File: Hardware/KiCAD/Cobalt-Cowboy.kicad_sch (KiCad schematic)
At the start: 1 part, among them P1 USB_C_Plug

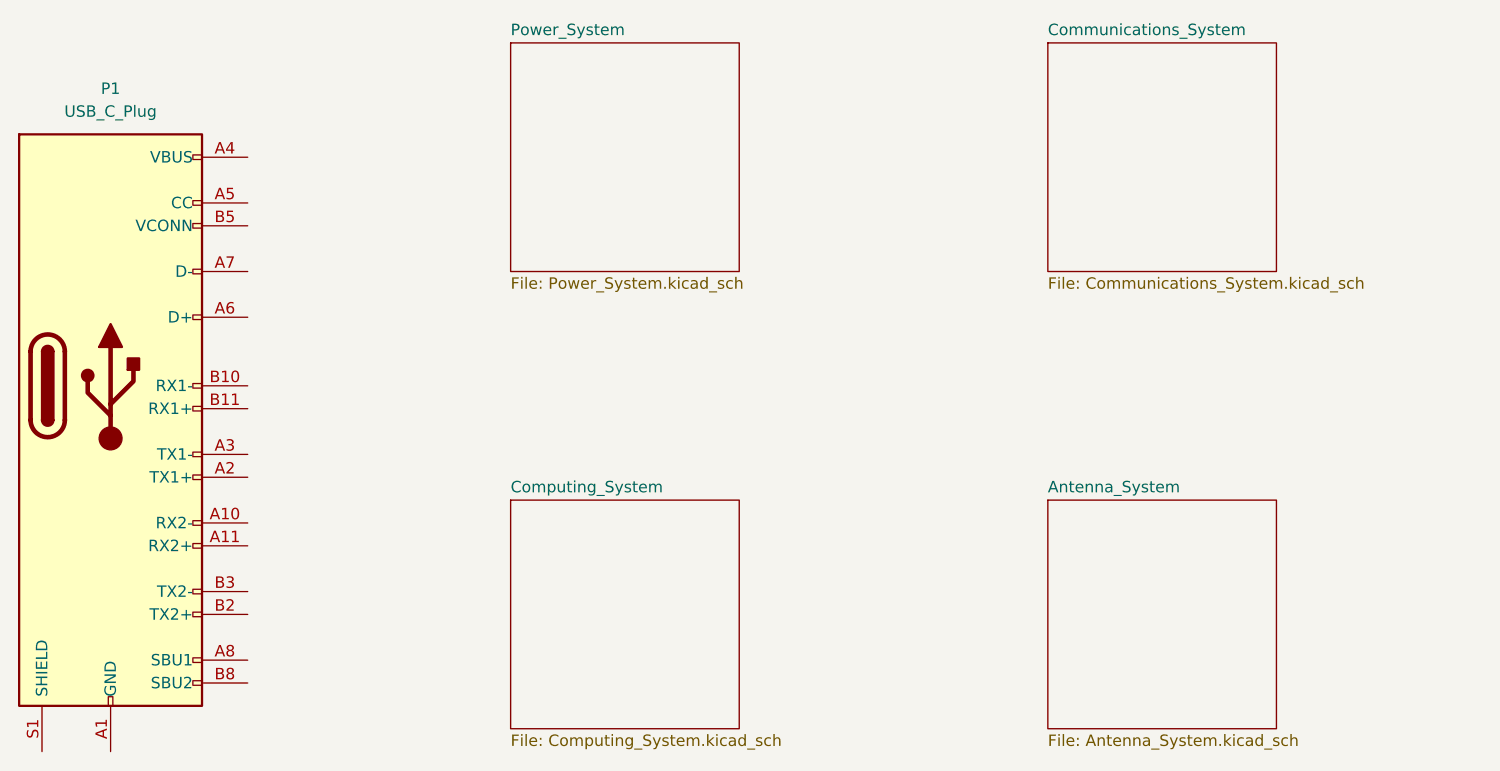
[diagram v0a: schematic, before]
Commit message: feat: add models, correct hierarchical patterns
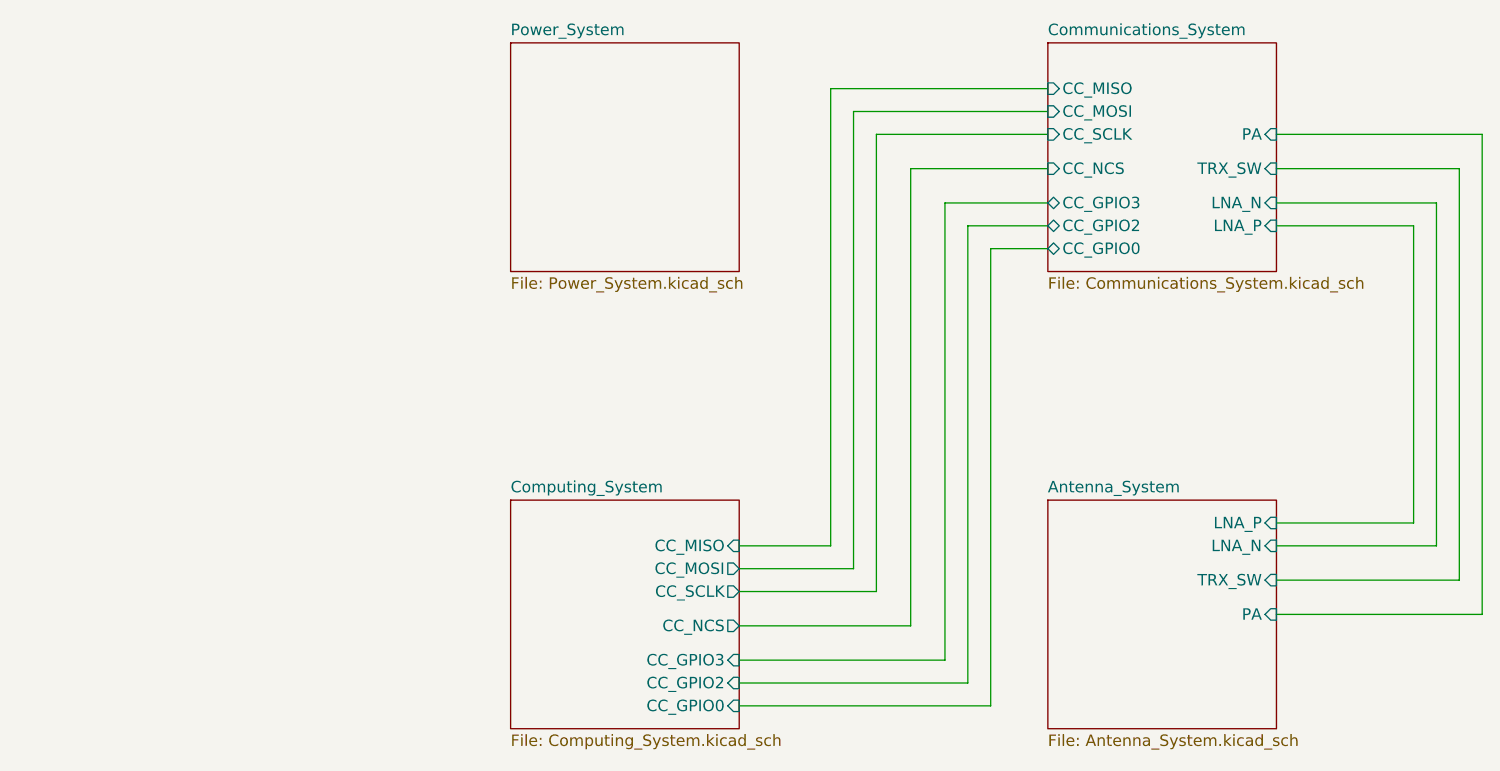
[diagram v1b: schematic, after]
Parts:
- removed P1: USB_C_Plug, symbol Connector:USB_C_Plug
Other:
- sheet Antenna_System ports: added LNA_N, LNA_P, PA, TRX_SW; removed none
- sheet Communications_System ports: added CC_GPIO0, CC_GPIO2, CC_GPIO3, CC_MISO, CC_MOSI, CC_NCS, CC_SCLK, LNA_N, LNA_P, PA, TRX_SW; removed none
- sheet Computing_System ports: added CC_GPIO0, CC_GPIO2, CC_GPIO3, CC_MISO, CC_MOSI, CC_NCS, CC_SCLK; removed none
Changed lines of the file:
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@@
 (kicad_sch (version 20230121) (generator eeschema)
   (paper "A4")
-  (symbol (lib_id "Connector:USB_C_Plug") (at 35.56 76.2 0) (unit 1)
-    (in_bom yes) (on_board yes) (dnp no) (fields_autoplaced)
-    (property "Reference" "P1" (at 35.56 43.18 0)
-      (effects (font (size 1.27 1.27)))
-    )
-    (property "Value" "USB_C_Plug" (at 35.56 45.72 0)
-      (effects (font (size 1.27 1.27)))
-    )
-    (property "Footprint" "" (at 39.37 76.2 0)
-      (effects (font (size 1.27 1.27)) hide)
-    )
-    (property "Datasheet" "https://www.usb.org/sites/default/files/documents/usb_type-c.zip" (at 39.37 76.2 0)
-      (effects (font (size 1.27 1.27)) hide)
-    )
-    (pin "A1")
-    (pin "A10")
-    (pin "A11")
-    (pin "A12")
-    (pin "A2")
-    (pin "A3")
-    (pin "A4")
-    (pin "A5")
-    (pin "A6")
-    (pin "A7")
-    (pin "A8")
-    (pin "A9")
-    (pin "B1")
-    (pin "B10")
-    (pin "B11")
-    (pin "B12")
-    (pin "B2")
-    (pin "B3")
-    (pin "B4")
-    (pin "B5")
-    (pin "B8")
-    (pin "B9")
-    (pin "S1")
-    (instances
-      (project "Cobalt-Cowboy"
-        (path "/60a68eb1-aa0f-414e-b03b-965ad6b52dab"
-          (reference "P1") (unit 1)
-        )
-      )
-    )
+  (wire (pts (xy 185.42 97.79) (xy 165.1 97.79))
+    (stroke (width 0) (type default))
+  )
+  (wire (pts (xy 187.96 101.6) (xy 165.1 101.6))
+    (stroke (width 0) (type default))
+  )
+  (wire (pts (xy 133.35 111.76) (xy 133.35 60.96))
+    (stroke (width 0) (type default))
+  )
+  (wire (pts (xy 124.46 52.07) (xy 139.7 52.07))
+    (stroke (width 0) (type default))
+  )
+  (wire (pts (xy 118.11 96.52) (xy 118.11 45.72))
+    (stroke (width 0) (type default))
+  )
+  (wire (pts (xy 120.65 99.06) (xy 120.65 48.26))
+    (stroke (width 0) (type default))
+  )
+  (wire (pts (xy 165.1 48.26) (xy 187.96 48.26))
+    (stroke (width 0) (type default))
+  )
+  (wire (pts (xy 182.88 55.88) (xy 182.88 93.98))
+    (stroke (width 0) (type default))
+  )
+  (wire (pts (xy 105.41 106.68) (xy 128.27 106.68))
+    (stroke (width 0) (type default))
+  )
+  (wire (pts (xy 115.57 43.18) (xy 139.7 43.18))
+    (stroke (width 0) (type default))
+  )
+  (wire (pts (xy 165.1 52.07) (xy 185.42 52.07))
+    (stroke (width 0) (type default))
+  )
+  (wire (pts (xy 128.27 106.68) (xy 128.27 55.88))
+    (stroke (width 0) (type default))
+  )
+  (wire (pts (xy 165.1 58.42) (xy 180.34 58.42))
+    (stroke (width 0) (type default))
+  )
+  (wire (pts (xy 124.46 102.87) (xy 124.46 52.07))
+    (stroke (width 0) (type default))
+  )
+  (wire (pts (xy 182.88 93.98) (xy 165.1 93.98))
+    (stroke (width 0) (type default))
+  )
+  (wire (pts (xy 120.65 48.26) (xy 139.7 48.26))
+    (stroke (width 0) (type default))
+  )
+  (wire (pts (xy 118.11 45.72) (xy 139.7 45.72))
+    (stroke (width 0) (type default))
+  )
+  (wire (pts (xy 105.41 99.06) (xy 120.65 99.06))
+    (stroke (width 0) (type default))
+  )
+  (wire (pts (xy 187.96 48.26) (xy 187.96 101.6))
+    (stroke (width 0) (type default))
+  )
+  (wire (pts (xy 105.41 102.87) (xy 124.46 102.87))
+    (stroke (width 0) (type default))
+  )
+  (wire (pts (xy 105.41 93.98) (xy 115.57 93.98))
+    (stroke (width 0) (type default))
+  )
+  (wire (pts (xy 128.27 55.88) (xy 139.7 55.88))
+    (stroke (width 0) (type default))
+  )
+  (wire (pts (xy 105.41 109.22) (xy 130.81 109.22))
+    (stroke (width 0) (type default))
+  )
+  (wire (pts (xy 180.34 91.44) (xy 165.1 91.44))
+    (stroke (width 0) (type default))
+  )
+  (wire (pts (xy 180.34 58.42) (xy 180.34 91.44))
+    (stroke (width 0) (type default))
+  )
+  (wire (pts (xy 185.42 52.07) (xy 185.42 97.79))
+    (stroke (width 0) (type default))
+  )
+  (wire (pts (xy 105.41 96.52) (xy 118.11 96.52))
+    (stroke (width 0) (type default))
+  )
+  (wire (pts (xy 105.41 111.76) (xy 133.35 111.76))
+    (stroke (width 0) (type default))
+  )
+  (wire (pts (xy 115.57 93.98) (xy 115.57 43.18))
+    (stroke (width 0) (type default))
+  )
+  (wire (pts (xy 130.81 58.42) (xy 139.7 58.42))
+    (stroke (width 0) (type default))
+  )
+  (wire (pts (xy 133.35 60.96) (xy 139.7 60.96))
+    (stroke (width 0) (type default))
+  )
+  (wire (pts (xy 165.1 55.88) (xy 182.88 55.88))
+    (stroke (width 0) (type default))
+  )
+  (wire (pts (xy 130.81 109.22) (xy 130.81 58.42))
+    (stroke (width 0) (type default))
   )
   (sheet (at 80.01 88.9) (size 25.4 25.4) (fields_autoplaced)
@@
       (effects (font (size 1.27 1.27)) (justify left top))
     )
+    (pin "CC_GPIO2" input (at 105.41 109.22 0)
+      (effects (font (size 1.27 1.27)) (justify right))
+    )
+    (pin "CC_GPIO3" input (at 105.41 106.68 0)
+      (effects (font (size 1.27 1.27)) (justify right))
+    )
+    (pin "CC_GPIO0" input (at 105.41 111.76 0)
+      (effects (font (size 1.27 1.27)) (justify right))
+    )
+    (pin "CC_NCS" output (at 105.41 102.87 0)
+      (effects (font (size 1.27 1.27)) (justify right))
+    )
+    (pin "CC_SCLK" output (at 105.41 99.06 0)
+      (effects (font (size 1.27 1.27)) (justify right))
+    )
+    (pin "CC_MOSI" output (at 105.41 96.52 0)
+      (effects (font (size 1.27 1.27)) (justify right))
+    )
+    (pin "CC_MISO" input (at 105.41 93.98 0)
+      (effects (font (size 1.27 1.27)) (justify right))
+    )
     (instances
       (project "Cobalt-Cowboy"
@@
       (effects (font (size 1.27 1.27)) (justify left top))
     )
+    (pin "TRX_SW" input (at 165.1 97.79 0)
+      (effects (font (size 1.27 1.27)) (justify right))
+    )
+    (pin "PA" input (at 165.1 101.6 0)
+      (effects (font (size 1.27 1.27)) (justify right))
+    )
+    (pin "LNA_P" input (at 165.1 91.44 0)
+      (effects (font (size 1.27 1.27)) (justify right))
+    )
+    (pin "LNA_N" input (at 165.1 93.98 0)
+      (effects (font (size 1.27 1.27)) (justify right))
+    )
     (instances
       (project "Cobalt-Cowboy"
@@
       (effects (font (size 1.27 1.27)) (justify left top))
     )
+    (pin "CC_GPIO0" bidirectional (at 139.7 60.96 180)
+      (effects (font (size 1.27 1.27)) (justify left))
+    )
+    (pin "PA" input (at 165.1 48.26 0)
+      (effects (font (size 1.27 1.27)) (justify right))
+    )
+    (pin "TRX_SW" input (at 165.1 52.07 0)
+      (effects (font (size 1.27 1.27)) (justify right))
+    )
+    (pin "LNA_P" input (at 165.1 58.42 0)
+      (effects (font (size 1.27 1.27)) (justify right))
+    )
+    (pin "LNA_N" input (at 165.1 55.88 0)
+      (effects (font (size 1.27 1.27)) (justify right))
+    )
+    (pin "CC_GPIO3" bidirectional (at 139.7 55.88 180)
+      (effects (font (size 1.27 1.27)) (justify left))
+    )
+    (pin "CC_GPIO2" bidirectional (at 139.7 58.42 180)
+      (effects (font (size 1.27 1.27)) (justify left))
+    )
+    (pin "CC_MISO" input (at 139.7 43.18 180)
+      (effects (font (size 1.27 1.27)) (justify left))
+    )
+    (pin "CC_NCS" input (at 139.7 52.07 180)
+      (effects (font (size 1.27 1.27)) (justify left))
+    )
+    (pin "CC_MOSI" input (at 139.7 45.72 180)
+      (effects (font (size 1.27 1.27)) (justify left))
+    )
+    (pin "CC_SCLK" input (at 139.7 48.26 180)
+      (effects (font (size 1.27 1.27)) (justify left))
+    )
     (instances

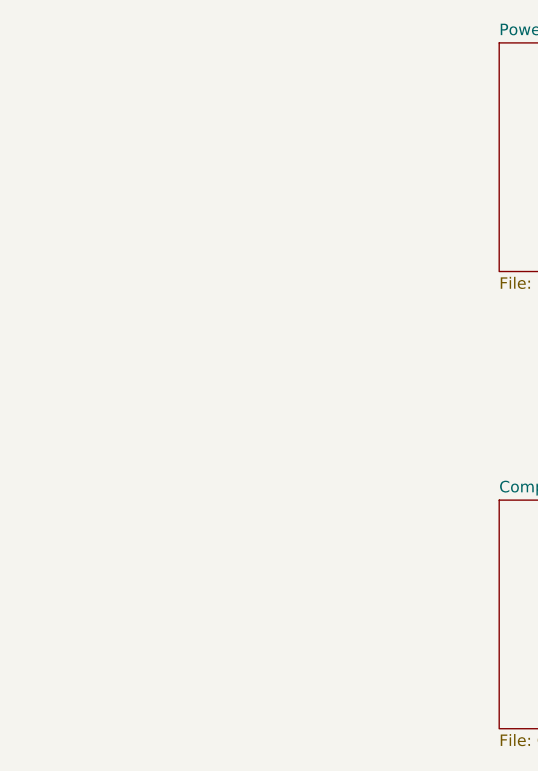
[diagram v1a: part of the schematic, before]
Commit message: added battery to start power systen
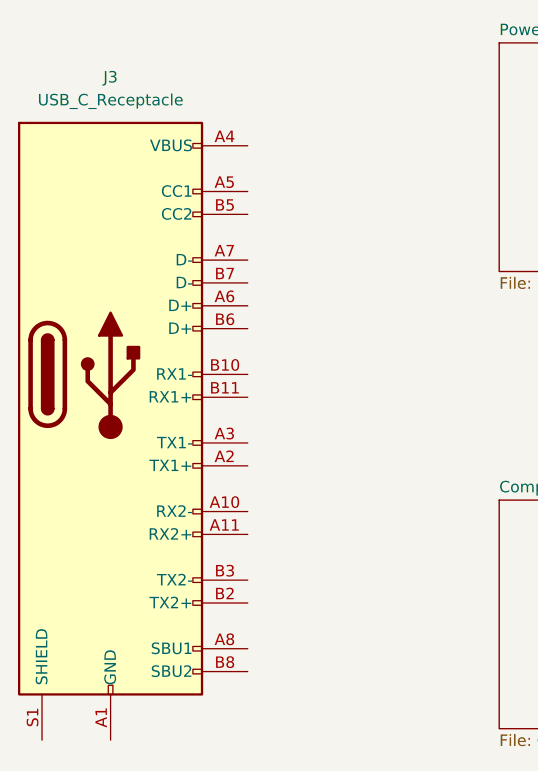
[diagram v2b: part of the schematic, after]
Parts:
- added J3: USB_C_Receptacle, Connector_USB:USB_C_Receptacle_GCT_USB4085, symbol Connector:USB_C_Receptacle
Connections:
- new net: J3.A1 (GND), J3.A12 (GND), J3.B1 (GND), J3.B12 (GND)
- new net: J3.A4 (VBUS), J3.A9 (VBUS), J3.B4 (VBUS), J3.B9 (VBUS)
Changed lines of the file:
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@@
     (stroke (width 0) (type default))
+  )
+  (symbol (lib_id "Connector:USB_C_Receptacle") (at 36.83 74.93 0) (unit 1)
+    (in_bom yes) (on_board yes) (dnp no) (fields_autoplaced)
+    (property "Reference" "J3" (at 36.83 41.91 0)
+      (effects (font (size 1.27 1.27)))
+    )
+    (property "Value" "USB_C_Receptacle" (at 36.83 44.45 0)
+      (effects (font (size 1.27 1.27)))
+    )
+    (property "Footprint" "Connector_USB:USB_C_Receptacle_GCT_USB4085" (at 40.64 74.93 0)
+      (effects (font (size 1.27 1.27)) hide)
+    )
+    (property "Datasheet" "https://www.usb.org/sites/default/files/documents/usb_type-c.zip" (at 40.64 74.93 0)
+      (effects (font (size 1.27 1.27)) hide)
+    )
+    (pin "A1")
+    (pin "A10")
+    (pin "A11")
+    (pin "A12")
+    (pin "A2")
+    (pin "A3")
+    (pin "A4")
+    (pin "A5")
+    (pin "A6")
+    (pin "A7")
+    (pin "A8")
+    (pin "A9")
+    (pin "B1")
+    (pin "B10")
+    (pin "B11")
+    (pin "B12")
+    (pin "B2")
+    (pin "B3")
+    (pin "B4")
+    (pin "B5")
+    (pin "B6")
+    (pin "B7")
+    (pin "B8")
+    (pin "B9")
+    (pin "S1")
+    (instances
+      (project "Cobalt-Cowboy"
+        (path "/60a68eb1-aa0f-414e-b03b-965ad6b52dab/f41c6f3a-9e23-419e-9eda-91d37d832739"
+          (reference "J3") (unit 1)
+        )
+        (path "/60a68eb1-aa0f-414e-b03b-965ad6b52dab"
+          (reference "J3") (unit 1)
+        )
+      )
+    )
   )
   (sheet (at 80.01 88.9) (size 25.4 25.4) (fields_autoplaced)

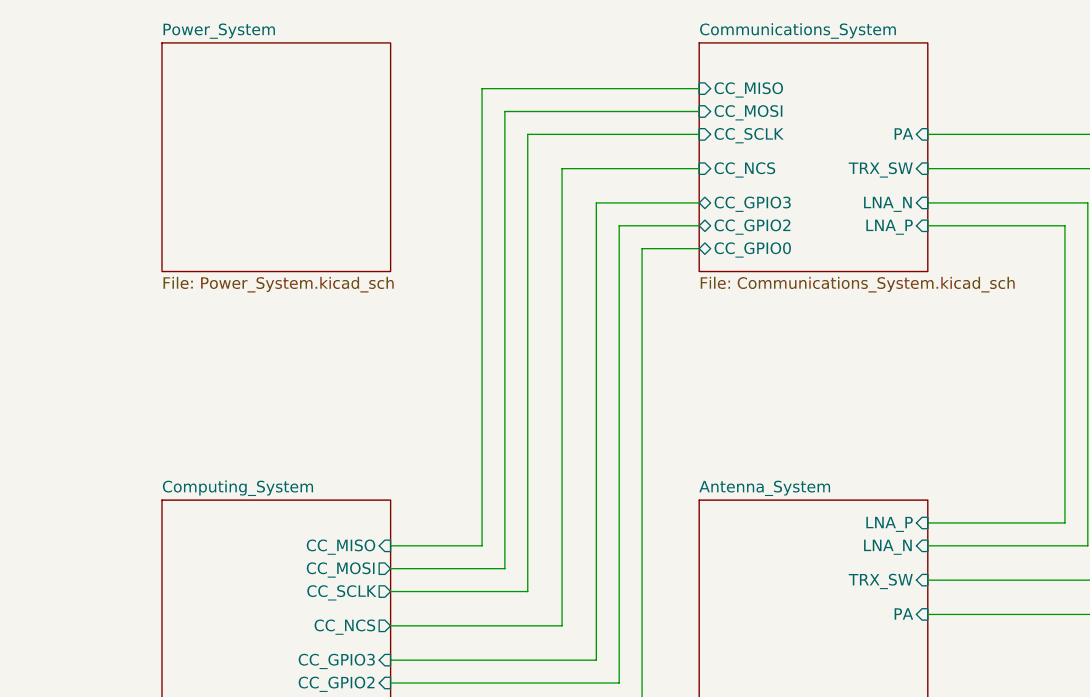
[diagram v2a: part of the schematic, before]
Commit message: Added components for amplifier, RF switch, 5v Boost, renamed footprints
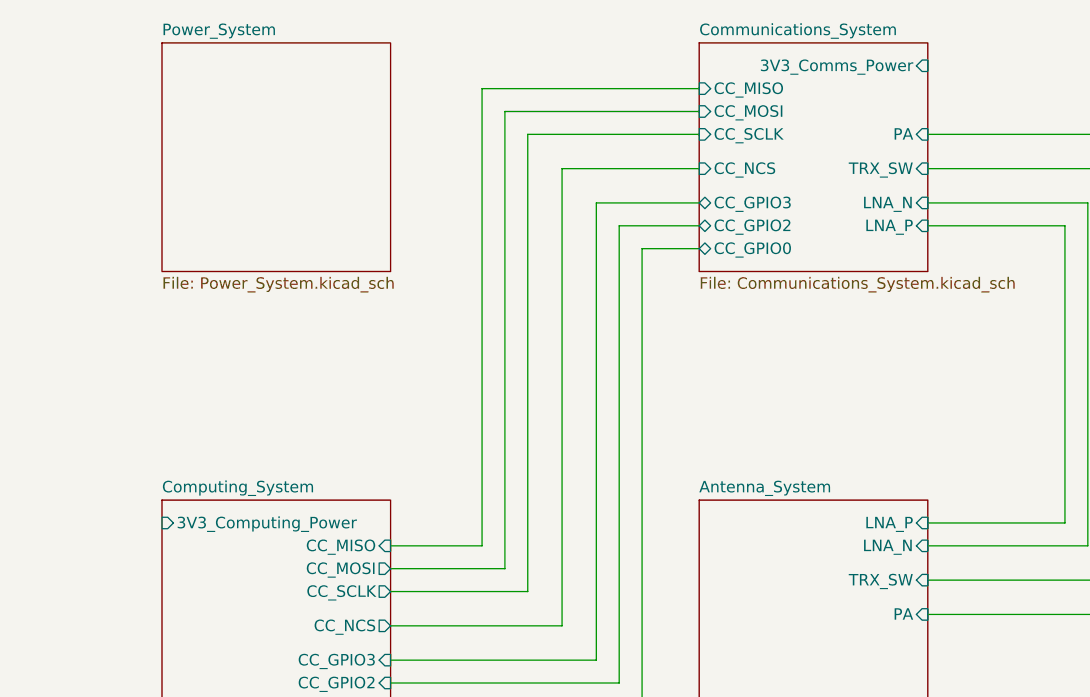
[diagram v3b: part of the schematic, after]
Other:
- sheet Communications_System ports: added 3V3_Comms_Power; removed none
- sheet Computing_System ports: added 3V3_Computing_Power; removed none
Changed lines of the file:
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@@
       (effects (font (size 1.27 1.27)) (justify right))
+    )
+    (pin "3V3_Computing_Power" input (at 80.01 91.44 180)
+      (effects (font (size 1.27 1.27)) (justify left))
     )
     (instances
@@
       (effects (font (size 1.27 1.27)) (justify left))
     )
+    (pin "3V3_Comms_Power" input (at 165.1 40.64 0)
+      (effects (font (size 1.27 1.27)) (justify right))
+    )
     (instances
